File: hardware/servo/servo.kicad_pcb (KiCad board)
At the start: 4 copper layers, 17 parts, among them U2 TPS54061DRBT, U3 DRV8876PWPR, U4 STM32G030F6P6, U5 SIT3088EEUA

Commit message: hardware
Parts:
- added C10: 100nF, Capacitor_SMD:C_0402_1005Metric, F.Cu at (75.0, 118.2)
- added C11: 22nF, Capacitor_SMD:C_0402_1005Metric, F.Cu at (65.3, 117.6)
- added C12: 220uF/50V, Capacitor_SMD:CP_Elec_10x10.5, F.Cu at (64.0, 106.8)
- added C13: 100nF, Capacitor_SMD:C_0402_1005Metric, F.Cu at (64.9, 116.2)
- added C7: 100nF, Capacitor_SMD:C_0402_1005Metric, F.Cu at (90.7, 111.5)
- added C8: 100nF, Capacitor_SMD:C_0402_1005Metric, F.Cu at (92.5, 116.5)
- added C9: 100nF, Capacitor_SMD:C_0402_1005Metric, F.Cu at (75.4, 121.0)
- added J2: Conn_ARM_SWD_TagConnect_TC2030-NL, Connector:Tag-Connect_TC2030-IDC-NL_2x03_P1.27mm_Vertical, F.Cu at (86.1, 113.0)
- added J3: Motor, Connector_JST:JST_PH_B2B-PH-K_1x02_P2.00mm_Vertical, F.Cu at (60.5, 116.6)
- added R10: 10k, Resistor_SMD:R_0402_1005Metric, F.Cu at (74.6, 114.4)
- added R11: 10k, Resistor_SMD:R_0402_1005Metric, F.Cu at (87.2, 122.0)
- added R12: 10k, Resistor_SMD:R_0402_1005Metric, F.Cu at (89.1, 122.0)
- added R13: 10k, Resistor_SMD:R_0402_1005Metric, F.Cu at (85.8, 118.7)
- added R14: 10k, Resistor_SMD:R_0402_1005Metric, F.Cu at (84.8, 118.7)
- added R7: 10k, Resistor_SMD:R_0402_1005Metric, F.Cu at (76.6, 114.4)
- added R8: 10k, Resistor_SMD:R_0402_1005Metric, F.Cu at (75.0, 117.2)
- added R9: 10k, Resistor_SMD:R_0402_1005Metric, F.Cu at (65.1, 119.2)
- moved U3 44.9 mm to (69.7, 117.0), turned to 180 degrees
- moved U5 37.3 mm to (89.6, 118.6)
- moved U4 31.1 mm to (80.0, 118.4)
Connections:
- U3 pad 1: unconnected-(U3-EN/IN1-Pad1) -> Net-(U3-EN/IN1)
- U3 pad 10: unconnected-(U3-OUT2-Pad10) -> Net-(J3-Pin_2)
- U3 pad 11: unconnected-(U3-VM-Pad11) -> VPP
- U3 pad 12: unconnected-(U3-VCP-Pad12) -> Net-(U3-VCP)
- U3 pad 13: unconnected-(U3-CPH-Pad13) -> Net-(U3-CPH)
- U3 pad 14: unconnected-(U3-CPL-Pad14) -> Net-(U3-CPL)
- U3 pad 15: unconnected-(U3-GND-Pad15) -> GND
- U3 pad 16: unconnected-(U3-PMODE-Pad16) -> Net-(U3-PMODE)
- U3 pad 17: unconnected-(U3-EP-Pad17) -> GND
- U3 pad 2: unconnected-(U3-PH/IN2-Pad2) -> Net-(U3-PH/IN2)
- U3 pad 3: unconnected-(U3-~{SLEEP}-Pad3) -> Net-(U3-~{SLEEP})
- U3 pad 4: unconnected-(U3-~{FAULT}-Pad4) -> /nFAULT
- U3 pad 5: unconnected-(U3-VREF-Pad5) -> GND
- U3 pad 7: unconnected-(U3-IMODE-Pad7) -> Net-(U3-IMODE)
- U3 pad 8: unconnected-(U3-OUT1-Pad8) -> Net-(J3-Pin_1)
- U3 pad 9: unconnected-(U3-PGND-Pad9) -> GND
- U4 pad 1: unconnected-(U4-PB7-Pad1) -> /nFAULT
- U4 pad 10: unconnected-(U4-VDD-Pad10) -> +3.3V
- U4 pad 12: unconnected-(U4-PA4-Pad12) -> Net-(U3-PH/IN2)
- U4 pad 14: unconnected-(U4-PA6-Pad14) -> Net-(U3-EN/IN1)
- U4 pad 17: unconnected-(U4-PA11-Pad17) -> Net-(U4-PA11)
- U4 pad 18: unconnected-(U4-PA12-Pad18) -> Net-(U4-PA12)
- U4 pad 19: unconnected-(U4-PA13/SWDIO-Pad19) -> Net-(J2-SWDIO)
- U4 pad 2: unconnected-(U4-PB8-Pad2) -> /SCL
- U4 pad 20: unconnected-(U4-PA14/SWCLK-Pad20) -> Net-(J2-SWCLK)
- U4 pad 3: unconnected-(U4-PB9-Pad3) -> /SDA
- U4 pad 4: unconnected-(U4-NRST-Pad4) -> Net-(J2-~{RESET})
- U4 pad 5: unconnected-(U4-VDDA-Pad5) -> +3.3V
- U4 pad 7: unconnected-(U4-PA1-Pad7) -> /DE
- U4 pad 9: unconnected-(U4-GND-Pad9) -> GND
- U5 pad 1: unconnected-(U5-RO-Pad1) -> Net-(U4-PA12)
- U5 pad 2: unconnected-(U5-~{RE}-Pad2) -> Net-(U5-~{RE})
- U5 pad 3: unconnected-(U5-DE-Pad3) -> /DE
- U5 pad 4: unconnected-(U5-DI-Pad4) -> Net-(U4-PA11)
- U5 pad 5: unconnected-(U5-GND-Pad5) -> GND
- U5 pad 8: unconnected-(U5-VCC-Pad8) -> +3.3V
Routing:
- net VPP: track 2.15 -> 23.1 mm
- net +3.3V: track 13.7 -> 32.1 mm, vias 0 -> 10
- net Net-(J3-Pin_1): track 0.00 -> 13.6 mm
- net Net-(J2-~{RESET}): track 0.00 -> 13.3 mm
- net GND: track 6.29 -> 19.1 mm, vias 8 -> 31
- net Net-(U3-EN/IN1): track 0.00 -> 12.2 mm, vias 0 -> 2
- net /DE: track 0.00 -> 12.2 mm, vias 0 -> 2
- net Net-(U3-PH/IN2): track 0.00 -> 11.6 mm, vias 0 -> 2
- net Net-(J3-Pin_2): track 0.00 -> 8.06 mm
- net Net-(U4-PA11): track 0.00 -> 7.54 mm
- net /nFAULT: track 0.00 -> 6.47 mm
- net Net-(J2-SWDIO): track 0.00 -> 5.58 mm
- net Net-(U4-PA12): track 0.00 -> 4.98 mm
- net Net-(J2-SWCLK): track 0.00 -> 4.04 mm
- net Net-(U5-~{RE}): track 0.00 -> 2.74 mm
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- added copper zone on In1.Cu, net +3.3V
- added copper zone on In2.Cu, net GND

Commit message: hardware
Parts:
- added D1: LED_R, LED_SMD:LED_0603_1608Metric, F.Cu at (90.0, 121.8)
- added JI2C1: Conn_01x04, Connector_JST:JST_PH_B4B-PH-K_1x04_P2.00mm_Vertical, F.Cu at (94.5, 110.0)
- added JLIM2: Limit, Connector_JST:JST_PH_B2B-PH-K_1x02_P2.00mm_Vertical, F.Cu at (95.7, 119.3)
- added JSERVO0: Conn_01x03, Connector_JST:JST_PH_B3B-PH-K_1x03_P2.00mm_Vertical, F.Cu at (53.6, 116.4)
- added JSERVO1: Conn_01x03, Connector_JST:JST_PH_B3B-PH-K_1x03_P2.00mm_Vertical, F.Cu at (46.6, 116.4)
- added JSERVO2: Conn_01x03, Connector_JST:JST_PH_B3B-PH-K_1x03_P2.00mm_Vertical, F.Cu at (53.6, 107.2)
- added JSERVO3: Conn_01x03, Connector_JST:JST_PH_B3B-PH-K_1x03_P2.00mm_Vertical, F.Cu at (46.6, 107.2)
- added R15: 1k, Resistor_SMD:R_0402_1005Metric, F.Cu at (87.5, 121.8)
- added R16: 100R, Resistor_SMD:R_0402_1005Metric, F.Cu at (53.8, 120.0)
- added R17: 100R, Resistor_SMD:R_0402_1005Metric, F.Cu at (53.8, 122.0)
- added R18: 100R, Resistor_SMD:R_0402_1005Metric, F.Cu at (47.4, 120.0)
- added R19: 100R, Resistor_SMD:R_0402_1005Metric, F.Cu at (47.4, 122.0)
- added R20: 10k, Resistor_SMD:R_0402_1005Metric, F.Cu at (92.8, 121.2)
- added U6: SRV05-4, Package_TO_SOT_SMD:SOT-23-6, F.Cu at (50.6, 121.0)
- moved R12 11.0 mm to (95.5, 113.0)
- moved R11 11.0 mm to (93.5, 113.0)
- renumbered J3 to JMOTOR2
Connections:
- U4 pad 11: unconnected-(U4-PA3-Pad11) -> /SERVO2
- U4 pad 13: unconnected-(U4-PA5-Pad13) -> /LED
- U4 pad 15: unconnected-(U4-PA7-Pad15) -> /SERVO3
- U4 pad 16: unconnected-(U4-PA8-Pad16) -> Net-(JLIM2-Pin_1)
- U4 pad 6: unconnected-(U4-PA0-Pad6) -> /SERVO0
- U4 pad 8: unconnected-(U4-PA2-Pad8) -> /SERVO1
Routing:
- net /SERVO3: track 0.00 -> 36.2 mm, vias 0 -> 2
- net /SERVO2: track 0.00 -> 34.7 mm, vias 0 -> 2
- net /SERVO1: track 0.00 -> 34.5 mm
- net /SERVO0: track 0.00 -> 33.5 mm
- net /SCL: track 0.00 -> 28.6 mm, vias 0 -> 2
- net /SDA: track 0.00 -> 25.0 mm, vias 0 -> 2
- net Net-(JLIM2-Pin_1): track 0.00 -> 20.9 mm, vias 0 -> 1
- net Net-(JSERVO3-Pin_2): track 0.00 -> 19.1 mm
- net Net-(JSERVO2-Pin_2): track 0.00 -> 17.7 mm
- net Net-(JSERVO0-Pin_2): track 0.00 -> 9.08 mm
- net Net-(JSERVO1-Pin_2): track 0.00 -> 8.63 mm
- net +3.3V: track 32.1 -> 37.1 mm, vias 10 -> 15
- net /LED: track 0.00 -> 4.86 mm
- net GND: track 19.1 -> 20.6 mm, vias 31 -> 47
- net Net-(D1-K): track 0.00 -> 1.20 mm
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- added copper zone on F.Cu, net GND
- added copper zone on In1.Cu, net VPP
- removed copper zone on B.Cu, net GND

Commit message: hardware
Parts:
- added D2: SS36, Diode_SMD:D_SMA, F.Cu at (62.0, 98.0)
- added H2: MountingHole, MountingHole:MountingHole_3.2mm_M3_Pad_TopBottom, F.Cu at (98.0, 92.0)
- added H3: MountingHole, MountingHole:MountingHole_3.2mm_M3_Pad_TopBottom, F.Cu at (62.0, 92.0)
- added H4: MountingHole, MountingHole:MountingHole_3.2mm_M3_Pad_TopBottom, F.Cu at (98.0, 126.0)
- added H5: MountingHole, MountingHole:MountingHole_3.2mm_M3_Pad_TopBottom, F.Cu at (62.0, 126.0)
- added JBUS1: Conn_01x04_XH, Connector_JST:JST_XH_S4B-XH-A_1x04_P2.50mm_Horizontal, F.Cu at (76.8, 97.4)
- added JBUS2: Conn_01x04_XH, Connector_JST:JST_XH_S4B-XH-A_1x04_P2.50mm_Horizontal, F.Cu at (90.8, 97.4)
- added JPWR2: Conn_01x02_XH, Connector_JST:JST_XH_S2B-XH-A_1x02_P2.50mm_Horizontal, F.Cu at (54.4, 93.8)
- moved R17 0.09 mm to (53.7, 122.0)
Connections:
- U5 pad 6: unconnected-(U5-A-Pad6) -> Net-(JBUS1-Pin_3)
- U5 pad 7: unconnected-(U5-B-Pad7) -> Net-(JBUS1-Pin_2)
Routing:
- net Net-(JBUS1-Pin_3): track 0.00 -> 41.3 mm, vias 0 -> 1
- net Net-(JBUS1-Pin_2): track 0.00 -> 40.1 mm, vias 0 -> 1
- net Net-(D2-A): track 0.00 -> 7.32 mm
- net GND: vias 47 -> 46
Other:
- board outline added: 59 x 43 mm

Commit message: updates
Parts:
- added C14: 10uF, Capacitor_SMD:C_0402_1005Metric, F.Cu at (90.6, 107.0)
- added JPTERM2: TERM, Jumper:SolderJumper-2_P1.3mm_Open_Pad1.0x1.5mm, F.Cu at (85.0, 124.0)
- added R21: 120R, Resistor_SMD:R_1206_3216Metric, F.Cu at (89.2, 124.0)
- moved H5 16.0 mm to (46.0, 127.0)
- moved H2 2.24 mm to (99.0, 90.0)
- moved H3 2.00 mm to (62.0, 90.0)
- moved H4 1.41 mm to (99.0, 127.0)
- moved JI2C1 1.15 mm to (95.7, 110.0)
- moved D1 0.20 mm to (90.0, 122.0)
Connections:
- net Net-(JBUS1-Pin_2) renamed /B
- net Net-(JBUS1-Pin_3) renamed /A
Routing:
- net /A: track 41.3 -> 52.8 mm
- net /B: track 40.1 -> 50.5 mm
- net Net-(JPTERM2-A): track 0.00 -> 2.09 mm
- net +3.3V: track 37.1 -> 38.9 mm
- net /SDA: track 25.0 -> 26.2 mm
- net Net-(JLIM2-Pin_1): track 20.9 -> 19.8 mm
- net GND: track 20.6 -> 21.2 mm, vias 46 -> 47
- added copper zone on B.Cu, net GND
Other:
- board size 59 x 43 mm -> 61 x 45 mm
- board text added: "+V"
- board text added: "3V3"
- board text added: "A"
- board text added: "B"
- board text added: "GND"
- board text added: "LIM"
- board text added: "SCL"
- board text added: "SDA"

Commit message: boms
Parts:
- removed R5: 143k, Resistor_SMD:R_0402_1005Metric
- removed R6: 36.5k, Resistor_SMD:R_0402_1005Metric
- added C25: 2.2uF, Capacitor_SMD:C_1206_3216Metric, F.Cu at (75.0, 102.2)
- added C26: 100nF, Capacitor_SMD:C_0603_1608Metric, F.Cu at (74.2, 104.2)
- added C27: 100nF, Capacitor_SMD:C_0402_1005Metric, F.Cu at (76.4, 108.5)
- added C28: 10uF, Capacitor_SMD:C_0805_2012Metric, F.Cu at (80.5, 106.5)
- added C29: 10uF, Capacitor_SMD:C_0805_2012Metric, F.Cu at (80.5, 104.5)
- added D3: SS36, Diode_SMD:D_SMA, F.Cu at (86.8, 102.2)
- added JP2: SolderJumper_3_Bridged12, Jumper:SolderJumper-3_P1.3mm_Bridged12_RoundedPad1.0x1.5mm, B.Cu at (50.0, 116.3)
- added JP3: SolderJumper_3_Bridged12, Jumper:SolderJumper-3_P1.3mm_Bridged12_RoundedPad1.0x1.5mm, B.Cu at (50.0, 107.3)
- added JP4: SolderJumper_3_Bridged12, Jumper:SolderJumper-3_P1.3mm_Bridged12_RoundedPad1.0x1.5mm, B.Cu at (57.4, 110.7)
- added L2: 10uH, Inductor_SMD:L_Changjiang_FNR4030S, F.Cu at (79.4, 110.5)
- added R22: 100k, Resistor_SMD:R_0402_1005Metric, F.Cu at (71.2, 103.9)
- added R23: 40.2k, Resistor_SMD:R_0402_1005Metric, F.Cu at (78.0, 104.5)
- added R24: 10k, Resistor_SMD:R_0402_1005Metric, F.Cu at (78.0, 106.5)
- added U7: LMR38020SDDAR, Package_SO:SOIC-8-1EP_3.9x4.9mm_P1.27mm_EP2.29x3mm, F.Cu at (72.8, 108.9)
- L1: footprint Inductor_SMD:L_6.3x6.3_H3 -> Inductor_SMD:L_Sunlord_SWPA4018S
- moved R2 20.4 mm to (101.0, 111.5)
- moved R3 20.4 mm to (101.0, 112.7)
- moved R4 17.4 mm to (93.9, 112.4)
- moved C5 17.4 mm to (94.5, 114.0)
- moved C6 17.4 mm to (95.1, 112.4)
- moved C2 15.1 mm to (89.5, 106.7)
- moved C3 15.1 mm to (94.5, 105.4)
- moved R1 15.1 mm to (89.2, 109.4)
- moved U2 15.1 mm to (92.5, 108.4)
- moved C1 15.0 mm to (87.4, 106.4)
- moved L1 13.3 mm to (97.5, 109.0)
- moved C14 11.5 mm to (102.0, 108.8)
- moved C4 11.5 mm to (101.0, 108.8)
- moved R11 8.54 mm to (96.5, 105.0)
- moved R12 8.54 mm to (98.5, 105.0)
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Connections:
- JBUS1 pad 1: VPP -> /<NO NET>
- JBUS2 pad 1: VPP -> /<NO NET>
- JSERVO0 pad 1: VPP -> /SP1
- JSERVO1 pad 1: VPP -> /SP1
- JSERVO2 pad 1: VPP -> /SP2
- JSERVO3 pad 1: VPP -> /SP2
- U2 pad 3: Net-(U2-EN) -> VPP
- U3 pad 11: VPP -> Net-(JP4-C)
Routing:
- net VPP: track 23.1 -> 49.6 mm, vias 14 -> 20
- net /<NO NET>: track 0.00 -> 19.5 mm
- net Net-(U7-FB): track 0.00 -> 16.0 mm, vias 0 -> 2
- net /SCL: track 28.7 -> 41.6 mm
- net Net-(JP4-C): track 0.00 -> 12.1 mm, vias 0 -> 3
- net +5V: track 0.00 -> 11.9 mm, vias 0 -> 20
- net /SDA: track 26.2 -> 37.2 mm
- net /B: track 50.5 -> 59.1 mm
- net /SP1: track 0.00 -> 7.08 mm
- net /SP2: track 0.00 -> 7.08 mm
- net Net-(U2-VSENSE): track 4.34 -> 9.98 mm, vias 0 -> 2
- net Net-(U2-EN): track 5.47 -> 0.00 mm
- net +3.3V: track 38.9 -> 33.6 mm, vias 15 -> 14
- net Net-(U7-BOOT): track 0.00 -> 4.87 mm
- net Net-(U7-RT/SYNC): track 0.00 -> 2.18 mm
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- added copper zone on F.Cu, net +5V
- added copper zone on In1.Cu, net +5V
- added copper zone on F.Cu, net Net-(JP4-C)
- added copper zone on F.Cu, net Net-(U7-SW)
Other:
- board size 61 x 45 mm -> 62 x 45 mm
- board text added: "12-36V"
- board text added: "5V"
- board text added: "5V 2A Limit, 3A V+ Limit"
- board text added: "DC Motor"
- board text added: "Servo 0-1"
- board text added: "Servo 2-3"
- board text added: "Tsumikoro Servo"
- board text added: "© 2026 StackFoundry LLC"

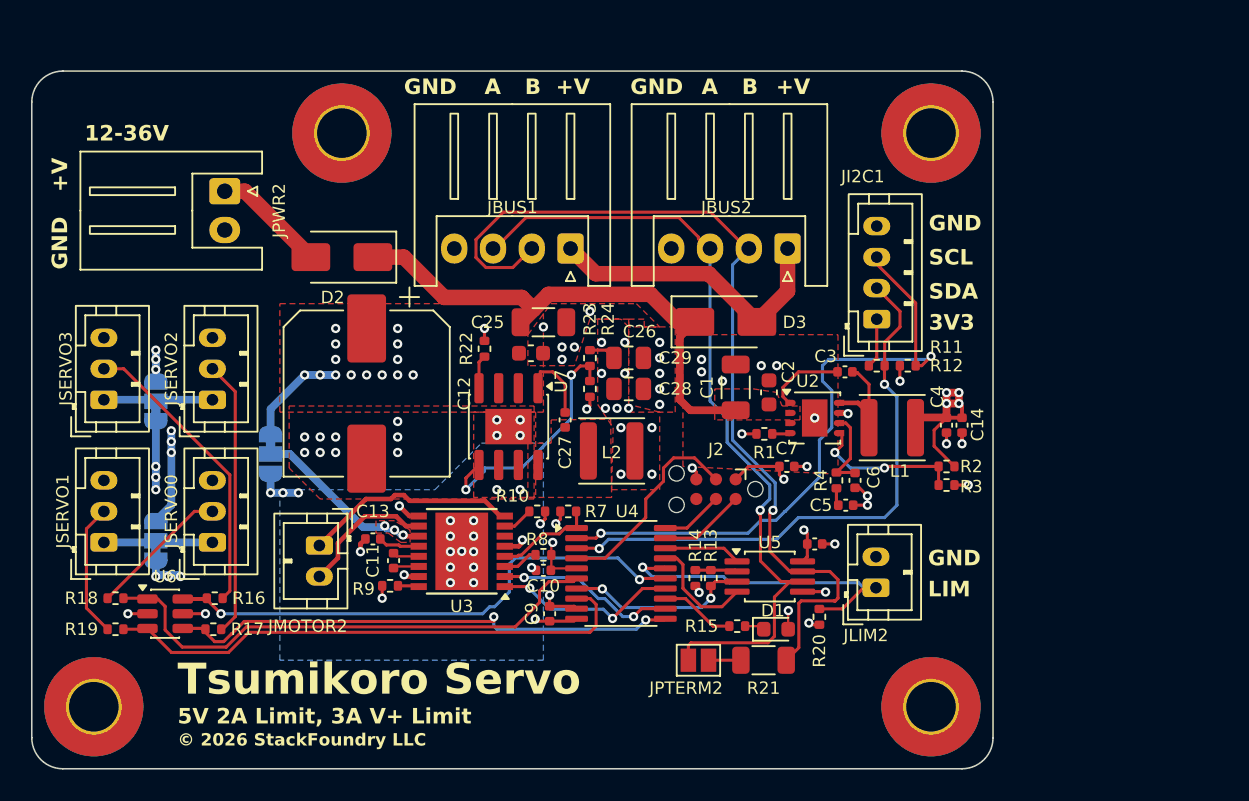
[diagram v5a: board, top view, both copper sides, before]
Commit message: hardware: regenerate servo docs + JLCPCB package
Refresh images, BOM, and manufacturing artifacts against the latest PCB
layout. Track the JLCPCB output directory and zip so the exact fab/assy
files shipped to the board-house are versioned alongside the design.

- Regenerated schematic + PCB SVGs and 3D renders
- Regenerated jlcpcb_bom.csv
- New hardware/servo/jlcpcb/ with gerbers, drill, BOM, CPL, README
- New hardware/servo/servo-jlcpcb.zip (single-file upload for JLCPCB)
- .gitignore: stop ignoring generated JLCPCB packages (now versioned)
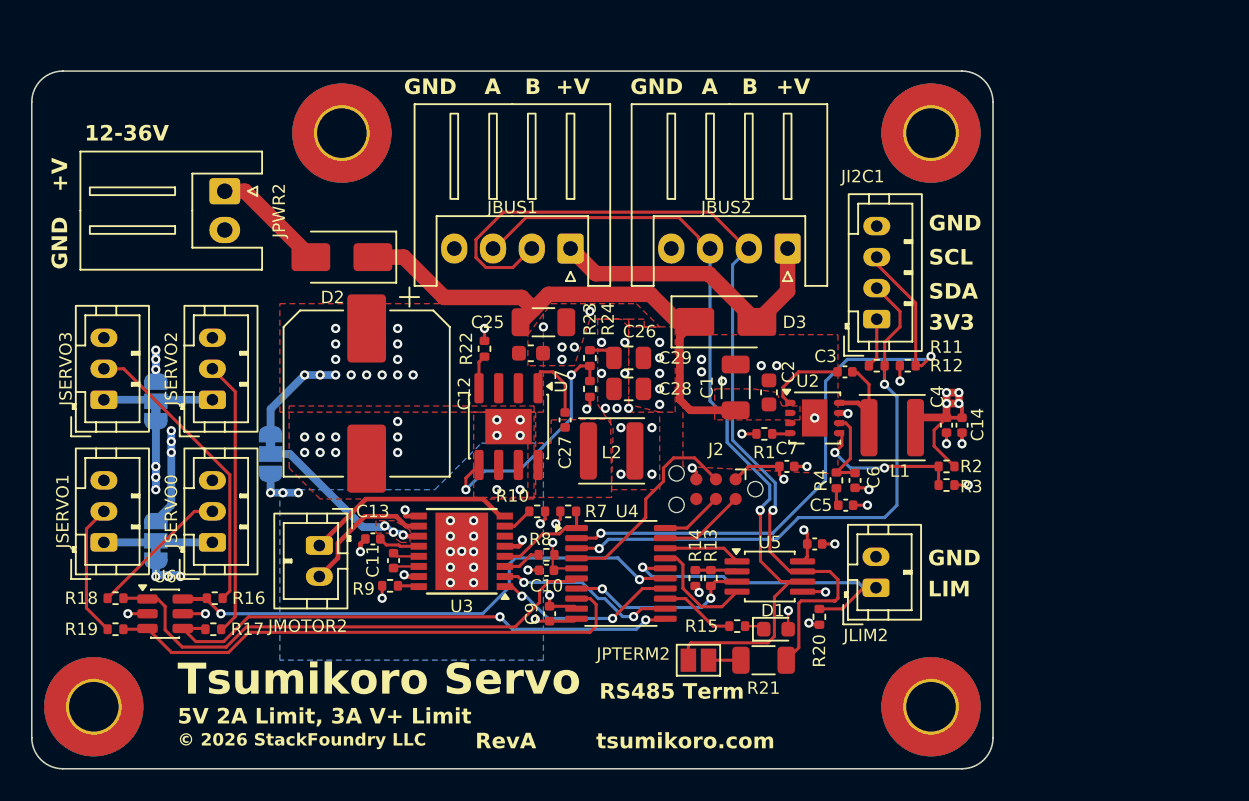
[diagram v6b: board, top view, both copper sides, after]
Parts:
- moved C10 0.20 mm to (75.2, 118.2)
- moved R8 0.20 mm to (75.2, 117.2)
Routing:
- net /SCL: track 41.6 -> 40.7 mm
- net /SERVO2: track 34.9 -> 34.3 mm
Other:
- board text added: "RS485 Term"
- board text added: "RevA"
- board text added: "tsumikoro.com"

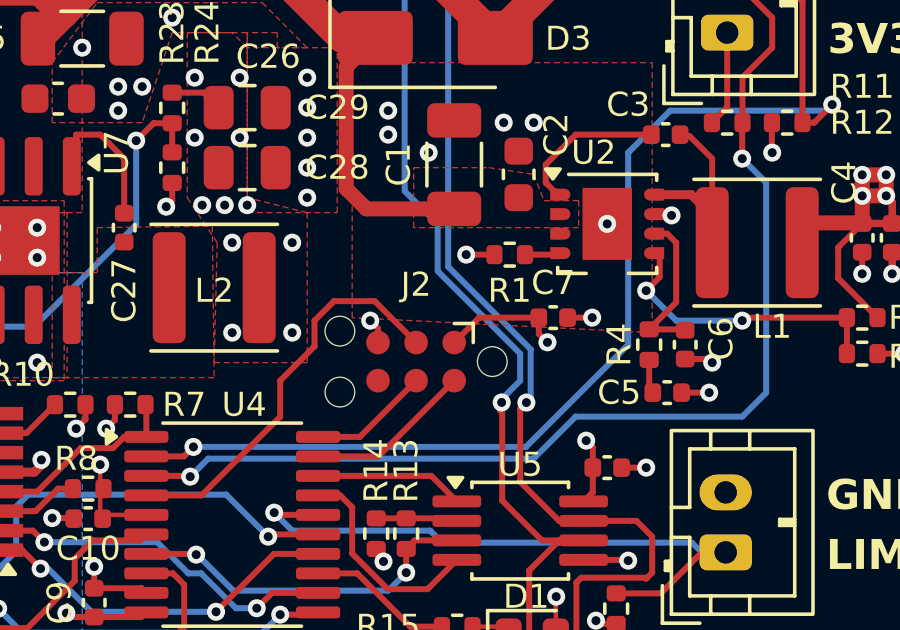
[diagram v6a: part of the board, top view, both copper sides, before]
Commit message: ministepper: finalize pin map + sync firmware to hardware rev 0.1
Hardware (schematic + docs) and firmware now share a single source of
truth for the STM32G071G8U6 UFQFPN-28 pinout:

- USART2 on PA2/PA3 (RS-485) — dedicated pins, no SYSCFG remap needed
  (unlike the servo's STM32G030 where PA11/PA12 shared pads with
  PA9/PA10)
- Two independent step timers: TIM1_CH1 on PA8 (STEP1) and TIM2_CH1
  on PA0 (STEP2) — each axis can run at its own rate
- Shared SPI1 (PA5/6/7) to both TMC2130s with software-managed CS on
  PA4 (TMC1) and PA12 (TMC2)
- Shared DRV_ENN on PA11 — pulls both drivers in/out of enable at once
- Per-axis limit switches (PB0, PB3) and DIAG1 stall/fault inputs
  (PB1, PB4)
- I2C1 on PB6/PB7 for expansion
- Status LED on PB5 (moved off PA5 which is now SPI SCK)
- 1 spare GPIO (PB8) for future use

firmware/tsumikoro-ministepper/src/main.c rewritten:
- Switched from USART1 to USART2; DMA request IDs updated
- PIN_* defines added for every pin from the schematic, cross-referenced
  to the hardware doc
- GPIO init configures all driver control lines (CS high, DRV_ENN high
  = off at boot), DIAG inputs, limit inputs with pull-ups, and the DE
  line for RS-485 (starts low = RX)
- Error_Handler moved to LED on PB5
- Bus callback extended to two-axis selector (byte 0 of move/stop
  payload picks axis 1 or 2); GET_STATUS reports both positions
- SPI1 / TIM1 / TIM2 stepper peripheral init still TODO — the real
  step generator will come with the SPI driver + per-axis motion
  planner

Hardware docs:
- CLAUDE.md adds "Ministepper PCB Pin Map" section (authoritative)
- hardware/ministepper/docs/README.md pin map updated to the final
  layout with independent STEP timers; sense-resistor variants
  (0.1 ohm standard vs 0.68 ohm micro / 28BYJ-48) documented
- hardware/TODO.md marks pin map + firmware sync done

Firmware builds clean (23 KB flash, 14.7 KB RAM) on STM32G071G8U6.
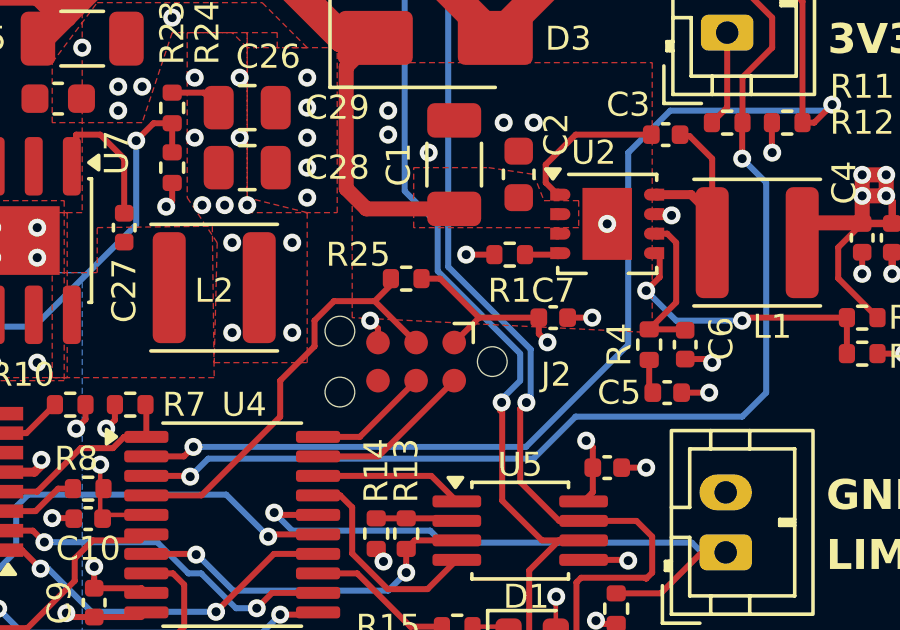
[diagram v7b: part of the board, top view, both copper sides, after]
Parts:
- added R25: 10k, Resistor_SMD:R_0402_1005Metric, F.Cu at (85.8, 110.2)
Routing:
- net +3.3V: track 33.3 -> 35.8 mm
- net Net-(J2-~{RESET}): track 13.5 -> 14.4 mm
